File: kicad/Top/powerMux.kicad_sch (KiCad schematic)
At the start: 4 parts

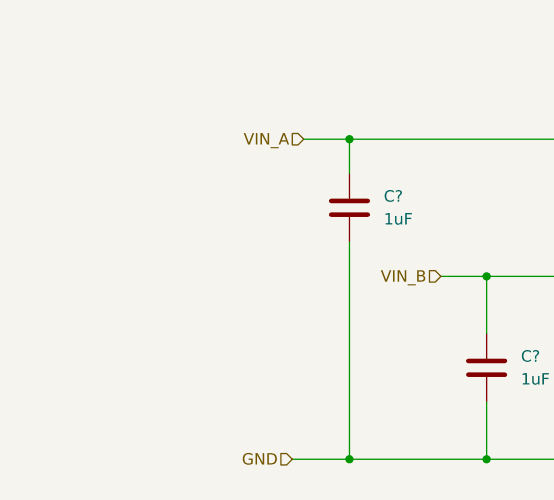
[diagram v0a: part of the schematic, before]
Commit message: Added note for power mux input priority
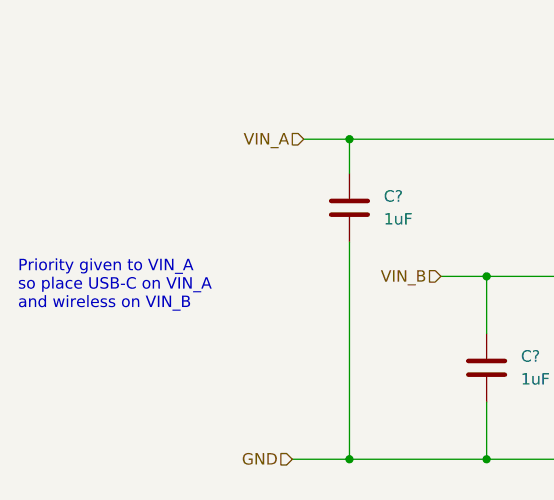
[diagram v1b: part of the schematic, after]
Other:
- note added: "Priority given to VIN_A so place USB-C on VIN_A and wireless on VIN_B"
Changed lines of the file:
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@@
+    (effects (font (size 1.27 1.27)) (justify left bottom))
+  )
+  (text "Priority given to VIN_A\nso place USB-C on VIN_A\nand wireless on VIN_B"
+    (at 59.69 107.95 0)
     (effects (font (size 1.27 1.27)) (justify left bottom))
   )

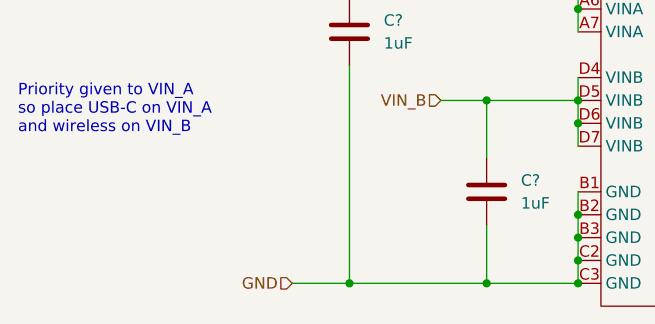
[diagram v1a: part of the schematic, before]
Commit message: Adding a few more higher level connections
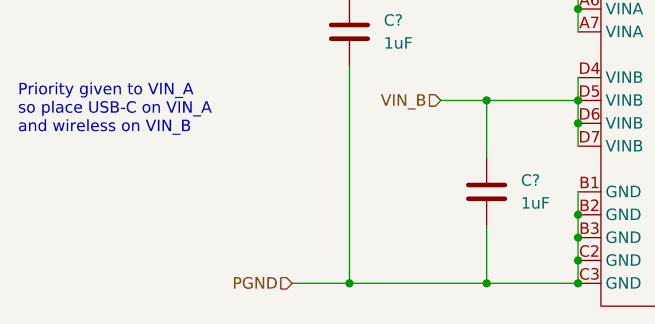
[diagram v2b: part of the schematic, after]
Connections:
- net GND: no longer C?.2, C?.2, U?.B1 (GND), U?.B2 (GND), U?.B3 (GND), U?.C2 (GND), U?.C3 (GND)
- new net PGND: C?.2, C?.2, U?.B1 (GND), U?.B2 (GND), U?.B3 (GND), U?.C2 (GND), U?.C3 (GND)
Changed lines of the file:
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@@
     (effects (font (size 1.27 1.27)) (justify left bottom))
   )
-  (hierarchical_label "GND" (shape input) (at 90.17 124.46 180)
+  (hierarchical_label "PGND" (shape input) (at 90.17 124.46 180)
     (effects (font (size 1.27 1.27)) (justify right))
   )

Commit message: wip
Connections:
- net VIN_B_EN/FLAG: no longer U?.D3 (VINB_EN/FLAG)
- new net FLAG: U?.D3 (VINB_EN/FLAG)
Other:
- note added: "Can range from 0V - VBattMax (4.2V?). Need to scale down to 3.3V. Should also protect with 3.3V Zener"
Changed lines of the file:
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@@
+    (stroke (width 0) (type default) (color 0 0 0 0))
+  )
+  (wire (pts (xy 45.72 148.59) (xy 35.56 148.59))
     (stroke (width 0) (type default) (color 0 0 0 0))
   )
@@
   )
   (wire (pts (xy 121.92 88.9) (xy 121.92 91.44))
+    (stroke (width 0) (type default) (color 0 0 0 0))
+  )
+  (wire (pts (xy 182.88 148.59) (xy 172.72 148.59))
     (stroke (width 0) (type default) (color 0 0 0 0))
   )
@@
     (stroke (width 0) (type default) (color 0 0 0 0))
   )
-  (text "FLAG used to report to MCU valid boolean voltage." (at 190.5 111.76 0)
+  (text "VINA_S used to report to MCU current limited analog voltage."
+    (at 222.25 149.86 0)
     (effects (font (size 1.27 1.27)) (justify left bottom))
   )
-  (text "VINA_S used to report to MCU current limited analog voltage."
-    (at 180.34 106.68 0)
+  (text "Can range from 0V - VBattMax (4.2V?). Need to scale down to 3.3V.\nShould also protect with 3.3V Zener"
+    (at 184.15 146.05 0)
     (effects (font (size 1.27 1.27)) (justify left bottom))
   )
@@
     (effects (font (size 1.27 1.27)) (justify left bottom))
   )
+  (text "FLAG used to report to MCU valid boolean voltage." (at 90.17 148.59 0)
+    (effects (font (size 1.27 1.27)) (justify left bottom))
+  )
   (text "Set MODE and CTRL to Low to enable unlocked autonomous mode"
     (at 177.8 104.14 0)
     (effects (font (size 1.27 1.27)) (justify left bottom))
+  )
+  (label "FLAG" (at 35.56 148.59 0)
+    (effects (font (size 1.27 1.27)) (justify left bottom))
+  )
+  (label "VINA_S" (at 172.72 148.59 0)
+    (effects (font (size 1.27 1.27)) (justify left bottom))
+  )
+  (label "FLAG" (at 170.18 111.76 180)
+    (effects (font (size 1.27 1.27)) (justify right bottom))
+  )
+  (label "VINA_S" (at 170.18 106.68 180)
+    (effects (font (size 1.27 1.27)) (justify right bottom))
   )
   (hierarchical_label "PGND" (shape input) (at 90.17 124.46 180)
@@
     (effects (font (size 1.27 1.27)) (justify right))
   )
+  (hierarchical_label "VIN_B_EN{slash}FLAG" (shape input) (at 72.39 148.59 0)
+    (effects (font (size 1.27 1.27)) (justify left))
+  )
+  (hierarchical_label "VINA_S" (shape input) (at 209.55 148.59 0)
+    (effects (font (size 1.27 1.27)) (justify left))
+  )
   (hierarchical_label "VOUT" (shape input) (at 176.53 88.9 0)
     (effects (font (size 1.27 1.27)) (justify left))
@@
     (effects (font (size 1.27 1.27)) (justify left))
   )
-  (hierarchical_label "VIN_B_EN{slash}FLAG" (shape input) (at 170.18 111.76 0)
-    (effects (font (size 1.27 1.27)) (justify left))
-  )
   (hierarchical_label "GND" (shape input) (at 170.18 104.14 0)
     (effects (font (size 1.27 1.27)) (justify left))
   )
-  (hierarchical_label "VINA_S" (shape input) (at 170.18 106.68 0)
-    (effects (font (size 1.27 1.27)) (justify left))
-  )

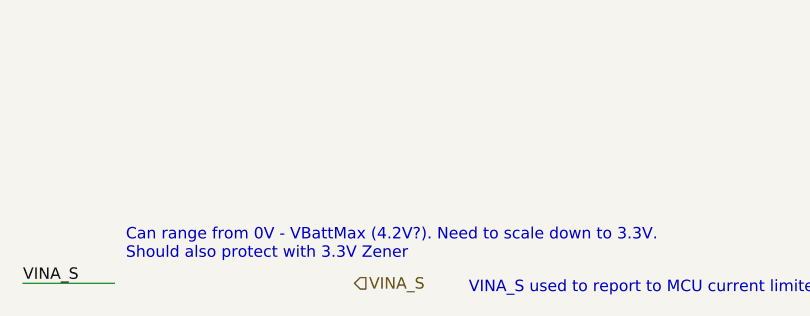
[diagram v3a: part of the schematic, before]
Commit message: Added overvoltage protection and filtering to ADC inputs of MCU
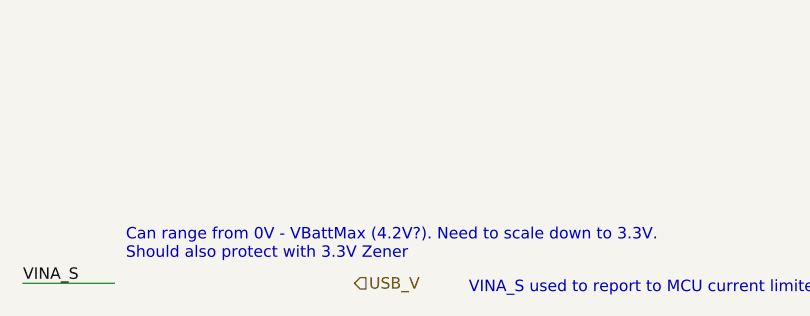
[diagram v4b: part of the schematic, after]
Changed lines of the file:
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@@
     (effects (font (size 1.27 1.27)) (justify left))
   )
-  (hierarchical_label "VINA_S" (shape input) (at 209.55 148.59 0)
+  (hierarchical_label "USB_V" (shape input) (at 209.55 148.59 0)
     (effects (font (size 1.27 1.27)) (justify left))
   )

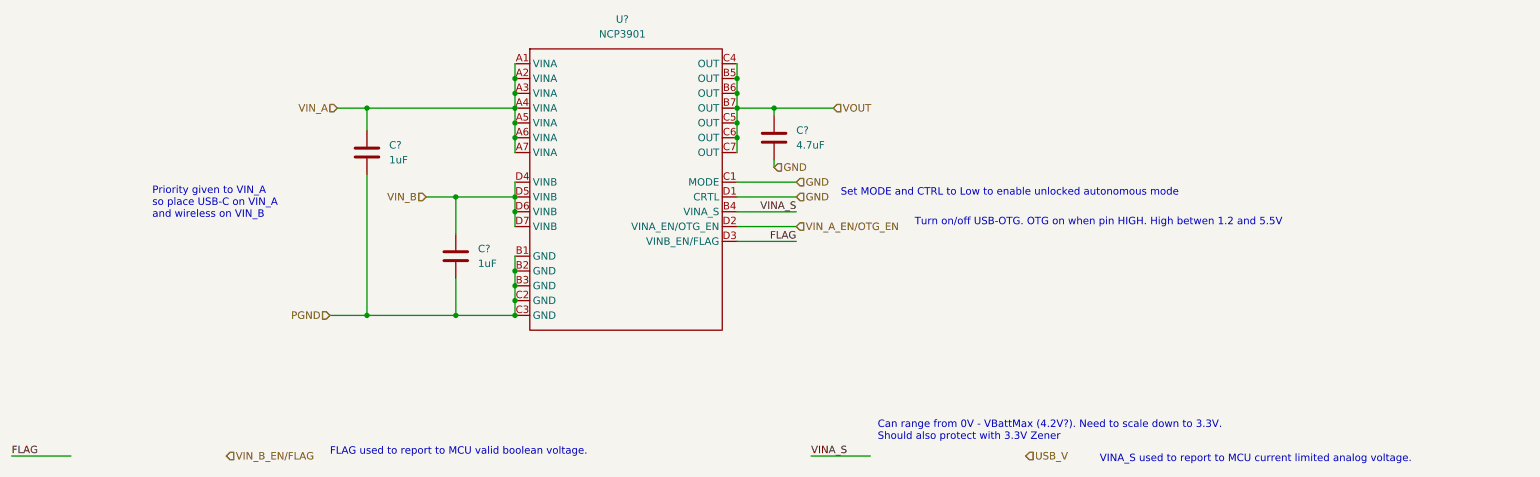
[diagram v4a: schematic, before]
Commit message: Wired up power mux MCU interfaces
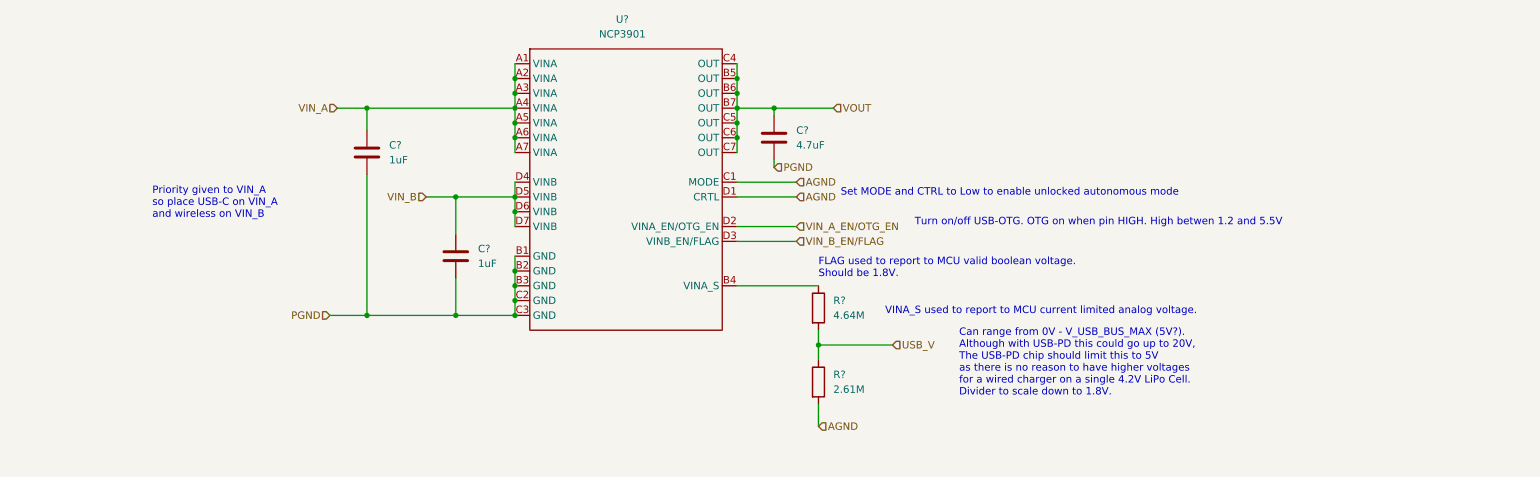
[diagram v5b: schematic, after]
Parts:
- added R?: 4.64M, symbol Device:R
- added R?: 2.61M, symbol Device:R
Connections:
- net FLAG is gone; now on net VIN_B_EN/FLAG: U?.D3 (VINB_EN/FLAG)
- net PGND: now also C?.2
- net USB_V: now also R?.1, R?.2
- net GND renamed AGND
- net AGND: now also R?.2; no longer C?.2
- net VINA_S: no longer names the net of U?.B4 (VINA_S)
- net VINA_S: now also R?.1
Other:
- note added: "Can range from 0V - V_USB_BUS_MAX (5V?). Although with USB-PD this could go up to 20V, The USB-PD chip should limit this to 5V as there is no reason to have higher voltages for a wired charger on a single 4.2V LiPo Cell. Divider to scale down to 1.8V."
- note added: "FLAG used to report to MCU valid boolean voltage. Should be 1.8V."
- note removed: "Can range from 0V - VBattMax (4.2V?). Need to scale down to 3.3V. Should also protect with 3.3V Zener"
- note removed: "FLAG used to report to MCU valid boolean voltage."
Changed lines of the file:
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@@
   (junction (at 121.92 124.46) (diameter 0) (color 0 0 0 0)
   )
+  (junction (at 173.99 129.54) (diameter 0) (color 0 0 0 0)
+  )
   (junction (at 160.02 88.9) (diameter 0) (color 0 0 0 0)
   )
@@
     (stroke (width 0) (type default) (color 0 0 0 0))
   )
+  (wire (pts (xy 173.99 129.54) (xy 173.99 132.08))
+    (stroke (width 0) (type default) (color 0 0 0 0))
+  )
   (wire (pts (xy 121.92 121.92) (xy 121.92 124.46))
     (stroke (width 0) (type default) (color 0 0 0 0))
@@
     (stroke (width 0) (type default) (color 0 0 0 0))
   )
+  (wire (pts (xy 173.99 127) (xy 173.99 129.54))
+    (stroke (width 0) (type default) (color 0 0 0 0))
+  )
   (wire (pts (xy 96.52 124.46) (xy 111.76 124.46))
     (stroke (width 0) (type default) (color 0 0 0 0))
@@
     (stroke (width 0) (type default) (color 0 0 0 0))
   )
-  (wire (pts (xy 45.72 148.59) (xy 35.56 148.59))
-    (stroke (width 0) (type default) (color 0 0 0 0))
-  )
   (wire (pts (xy 121.92 81.28) (xy 121.92 83.82))
     (stroke (width 0) (type default) (color 0 0 0 0))
@@
     (stroke (width 0) (type default) (color 0 0 0 0))
   )
-  (wire (pts (xy 182.88 148.59) (xy 172.72 148.59))
-    (stroke (width 0) (type default) (color 0 0 0 0))
-  )
-  (wire (pts (xy 160.02 106.68) (xy 170.18 106.68))
+  (wire (pts (xy 160.02 119.38) (xy 173.99 119.38))
     (stroke (width 0) (type default) (color 0 0 0 0))
   )
@@
     (stroke (width 0) (type default) (color 0 0 0 0))
   )
+  (wire (pts (xy 173.99 129.54) (xy 186.69 129.54))
+    (stroke (width 0) (type default) (color 0 0 0 0))
+  )
+  (wire (pts (xy 173.99 139.7) (xy 173.99 143.51))
+    (stroke (width 0) (type default) (color 0 0 0 0))
+  )
   (wire (pts (xy 111.76 118.11) (xy 111.76 124.46))
     (stroke (width 0) (type default) (color 0 0 0 0))
@@
   )
   (text "VINA_S used to report to MCU current limited analog voltage."
-    (at 222.25 149.86 0)
-    (effects (font (size 1.27 1.27)) (justify left bottom))
-  )
-  (text "Can range from 0V - VBattMax (4.2V?). Need to scale down to 3.3V.\nShould also protect with 3.3V Zener"
-    (at 184.15 146.05 0)
+    (at 185.42 124.46 0)
+    (effects (font (size 1.27 1.27)) (justify left bottom))
+  )
+  (text "Can range from 0V - V_USB_BUS_MAX (5V?). \nAlthough with USB-PD this could go up to 20V,\nThe USB-PD chip should limit this to 5V\nas there is no reason to have higher voltages\nfor a wired charger on a single 4.2V LiPo Cell.\nDivider to scale down to 1.8V.\n"
+    (at 198.12 138.43 0)
     (effects (font (size 1.27 1.27)) (justify left bottom))
   )
@@
     (effects (font (size 1.27 1.27)) (justify left bottom))
   )
-  (text "FLAG used to report to MCU valid boolean voltage." (at 90.17 148.59 0)
+  (text "FLAG used to report to MCU valid boolean voltage.\nShould be 1.8V. "
+    (at 173.99 118.11 0)
     (effects (font (size 1.27 1.27)) (justify left bottom))
   )
@@
     (effects (font (size 1.27 1.27)) (justify left bottom))
   )
-  (label "FLAG" (at 35.56 148.59 0)
-    (effects (font (size 1.27 1.27)) (justify left bottom))
-  )
-  (label "VINA_S" (at 172.72 148.59 0)
-    (effects (font (size 1.27 1.27)) (justify left bottom))
-  )
-  (label "FLAG" (at 170.18 111.76 180)
-    (effects (font (size 1.27 1.27)) (justify right bottom))
-  )
-  (label "VINA_S" (at 170.18 106.68 180)
-    (effects (font (size 1.27 1.27)) (justify right bottom))
-  )
   (hierarchical_label "PGND" (shape input) (at 90.17 124.46 180)
     (effects (font (size 1.27 1.27)) (justify right))
   )
-  (hierarchical_label "GND" (shape input) (at 170.18 101.6 0)
+  (hierarchical_label "AGND" (shape input) (at 170.18 101.6 0)
     (effects (font (size 1.27 1.27)) (justify left))
   )
@@
     (effects (font (size 1.27 1.27)) (justify right))
   )
-  (hierarchical_label "VIN_B_EN{slash}FLAG" (shape input) (at 72.39 148.59 0)
-    (effects (font (size 1.27 1.27)) (justify left))
-  )
-  (hierarchical_label "USB_V" (shape input) (at 209.55 148.59 0)
+  (hierarchical_label "VIN_B_EN{slash}FLAG" (shape input) (at 170.18 111.76 0)
+    (effects (font (size 1.27 1.27)) (justify left))
+  )
+  (hierarchical_label "AGND" (shape input) (at 170.18 104.14 0)
+    (effects (font (size 1.27 1.27)) (justify left))
+  )
+  (hierarchical_label "USB_V" (shape input) (at 186.69 129.54 0)
     (effects (font (size 1.27 1.27)) (justify left))
   )
@@
     (effects (font (size 1.27 1.27)) (justify left))
   )
-  (hierarchical_label "GND" (shape input) (at 170.18 104.14 0)
-    (effects (font (size 1.27 1.27)) (justify left))
-  )
-  (hierarchical_label "GND" (shape input) (at 166.37 99.06 0)
-    (effects (font (size 1.27 1.27)) (justify left))
+  (hierarchical_label "AGND" (shape input) (at 173.99 143.51 0)
+    (effects (font (size 1.27 1.27)) (justify left))
+  )
+  (hierarchical_label "PGND" (shape input) (at 166.37 99.06 0)
+    (effects (font (size 1.27 1.27)) (justify left))
+  )
+  (symbol (lib_id "Device:R") (at 173.99 123.19 0) (unit 1)
+    (in_bom yes) (on_board yes) (fields_autoplaced)
+    (property "Reference" "R?" (id 0) (at 176.53 121.9199 0)
+      (effects (font (size 1.27 1.27)) (justify left))
+    )
+    (property "Value" "4.64M" (id 1) (at 176.53 124.4599 0)
+      (effects (font (size 1.27 1.27)) (justify left))
+    )
+    (property "Footprint" "" (id 2) (at 172.212 123.19 90)
+      (effects (font (size 1.27 1.27)) hide)
+    )
+    (property "Datasheet" "~" (id 3) (at 173.99 123.19 0)
+      (effects (font (size 1.27 1.27)) hide)
+    )
+    (pin "1")
+    (pin "2")
   )
   (symbol (lib_id "Device:C") (at 166.37 93.98 0) (unit 1)
@@
     (pin "D7")
   )
+  (symbol (lib_id "Device:R") (at 173.99 135.89 0) (unit 1)
+    (in_bom yes) (on_board yes) (fields_autoplaced)
+    (property "Reference" "R?" (id 0) (at 176.53 134.6199 0)
+      (effects (font (size 1.27 1.27)) (justify left))
+    )
+    (property "Value" "2.61M" (id 1) (at 176.53 137.1599 0)
+      (effects (font (size 1.27 1.27)) (justify left))
+    )
+    (property "Footprint" "" (id 2) (at 172.212 135.89 90)
+      (effects (font (size 1.27 1.27)) hide)
+    )
+    (property "Datasheet" "~" (id 3) (at 173.99 135.89 0)
+      (effects (font (size 1.27 1.27)) hide)
+    )
+    (pin "1")
+    (pin "2")
+  )
 )
